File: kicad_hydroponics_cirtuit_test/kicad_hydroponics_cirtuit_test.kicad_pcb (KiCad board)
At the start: 2 copper layers, 8 parts, among them Q1 IRLZ34N

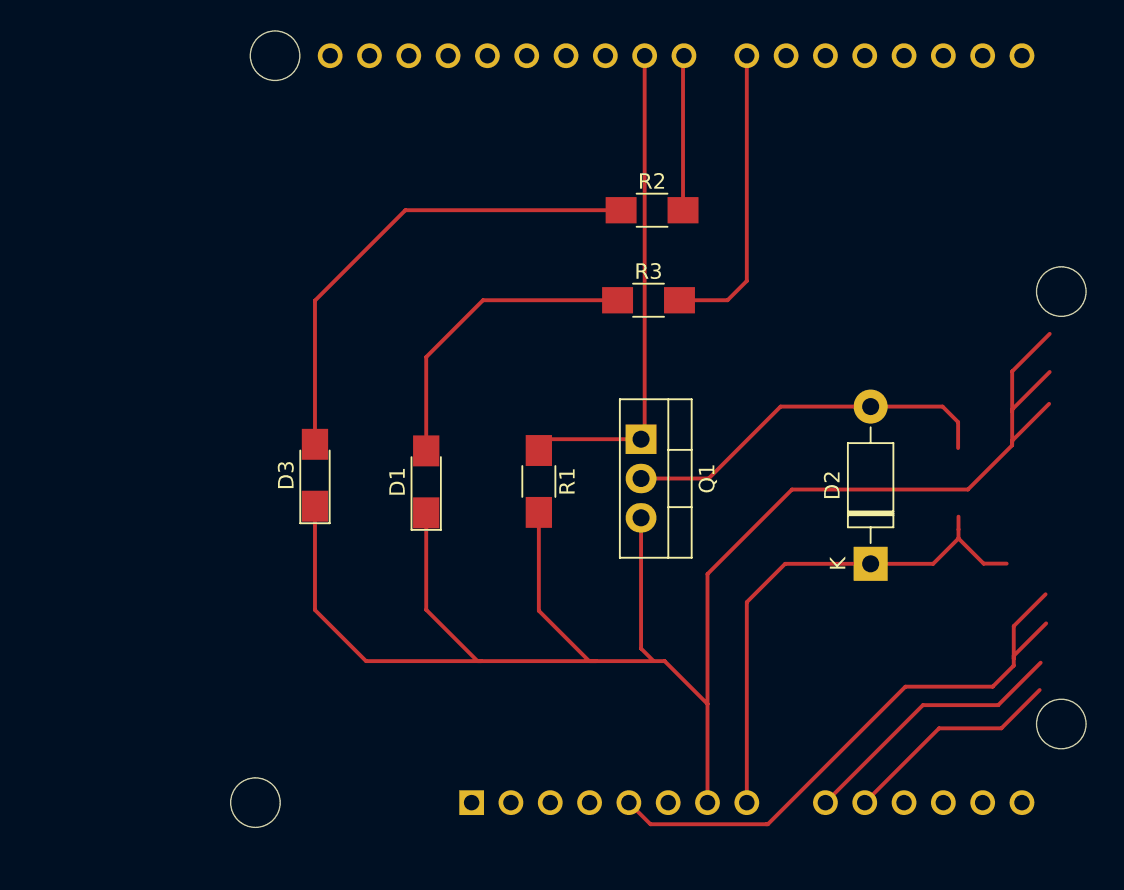
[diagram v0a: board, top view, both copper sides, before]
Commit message: Updated to use SMD components except diode 1N4007 is through hole. Water level sensor powering from Arduino digital pins to prevent sensor electrochemical corrosion
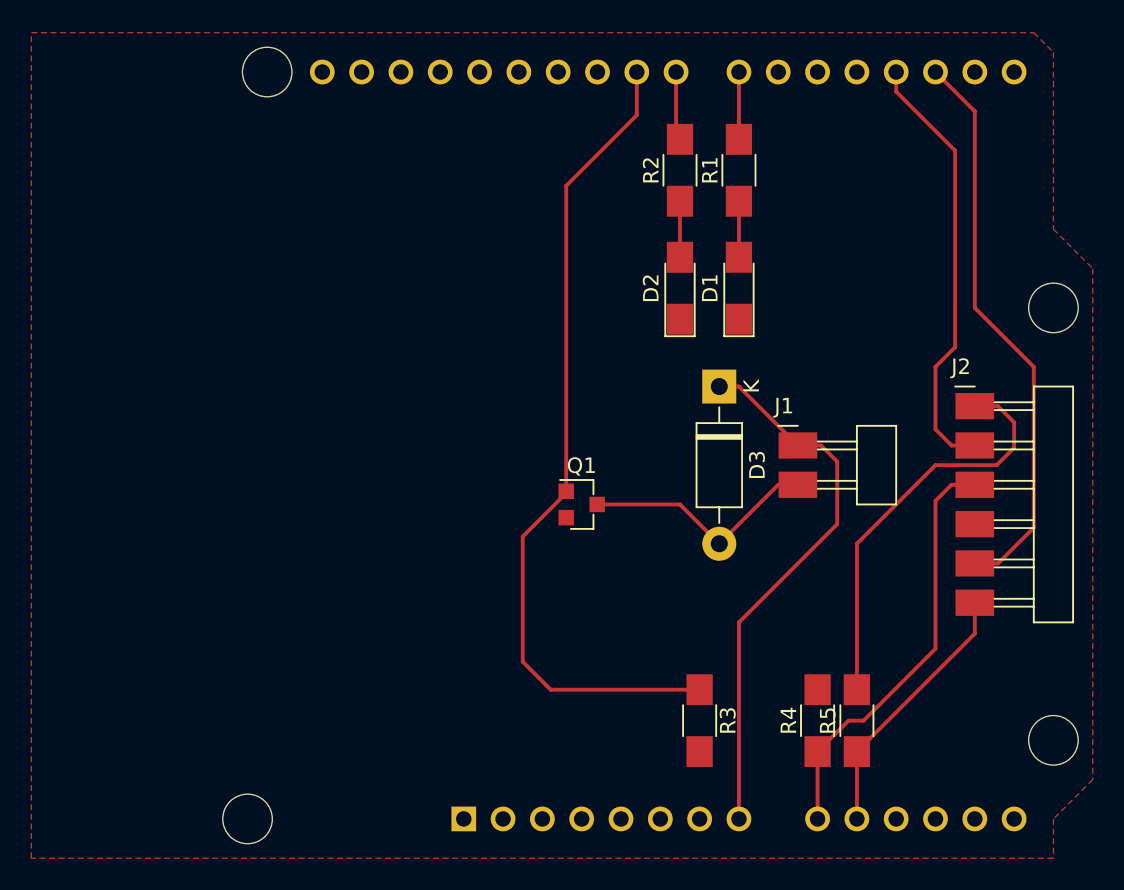
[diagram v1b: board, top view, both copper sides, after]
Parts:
- removed the R3 at (170.7, 70.6)
- added J1: Conn_01x02_Male, fab:Header_SMD_01x02_P2.54mm_Horizontal_Male, F.Cu at (180.3, 80.0)
- added J2: Conn_01x06_Male, fab:Header_SMD_01x06_P2.54mm_Horizontal_Male, F.Cu at (191.8, 77.5)
- added R1: R, fab:R_1206, F.Cu at (176.5, 62.2)
- added R4: R, fab:R_1206, F.Cu at (181.6, 97.8)
- added R5: R, fab:R_1206, F.Cu at (184.2, 97.8)
- Q1: value IRLZ34N -> MOSFET_N-CH_30V_1.7A; footprint Package_TO_SOT_THT:TO-220-3_Vertical -> fab:SOT-23
- moved D2 26.5 mm to (172.7, 69.8)
- moved D1 23.8 mm to (176.5, 69.8)
- moved R3 18.6 mm to (174.0, 97.8)
- moved D3 15.1 mm to (175.3, 76.2), turned to 270 degrees
- moved Q1 5.70 mm to (166.4, 83.8), turned to 0 degrees
- moved R2 3.15 mm to (172.7, 62.2), turned to 90 degrees
- moved A1 1.17 mm to (158.8, 104.1)
- renumbered D3 to D2, D2 to D3, R1 to R3
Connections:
- A1 pad 7: Net-(A1-Pad7) -> GND
- D1 pad 1: Net-(A1-Pad7) -> GND
- D2 pad 1: Net-(A1-Pad7) -> GND
- D3 pad 2: Net-(D2-Pad2) (its old number) -> Net-(D3-Pad2)
- Q1 pad 2: Net-(D2-Pad2) (its old number) -> GND
- Q1 pad 3: Net-(A1-Pad7) -> Net-(D3-Pad2)
- R3 pad 2: Net-(A1-Pad7) -> GND
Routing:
- net Net-(A1-Pad7): track 119.9 -> 0.00 mm
- net Net-(A1-Pad5): track 38.3 -> 0.00 mm
- net Net-(A1-Pad17): track 0.00 -> 38.1 mm
- net Net-(A1-Pad18): track 0.00 -> 28.2 mm
- net Net-(D2-Pad2): track 31.5 -> 3.62 mm
- net GND: track 0.00 -> 26.8 mm
- net Net-(D2-Pad2) (its old number): track 24.5 -> 0.00 mm
- net Net-(A1-Pad24): track 31.8 -> 53.3 mm
- net Net-(D1-Pad2): track 19.9 -> 3.62 mm
- net Net-(D3-Pad2): track 0.00 -> 15.6 mm
- net Net-(A1-Pad22): track 19.4 -> 4.35 mm
- net Net-(A1-Pad9): track 17.7 -> 27.2 mm
- net Net-(A1-Pad23): track 10.0 -> 4.81 mm
- net Net-(A1-Pad10): track 14.3 -> 17.9 mm
- net Net-(A1-Pad8): track 33.5 -> 35.3 mm
- added copper zone on F.Cu, net GND

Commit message: Add gerber files
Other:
- board outline added: 68.6 x 53.3 mm
